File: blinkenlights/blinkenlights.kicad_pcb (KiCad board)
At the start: 4 copper layers, 160 x 100 mm, 114 parts, among them J201 Conn_03x32_Row_Letter_First, J202 Conn_02x20_Odd_Even, J203 Conn_02x20_Odd_Even, J204 Conn_02x20_Odd_Even, J205 Conn_02x20_Odd_Even, J301 Conn_01x01_Female, J302 Conn_01x01_Female, J303 Conn_01x01_Female, U201 AT24CS32-SSHM, U301 BD9C301FJ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

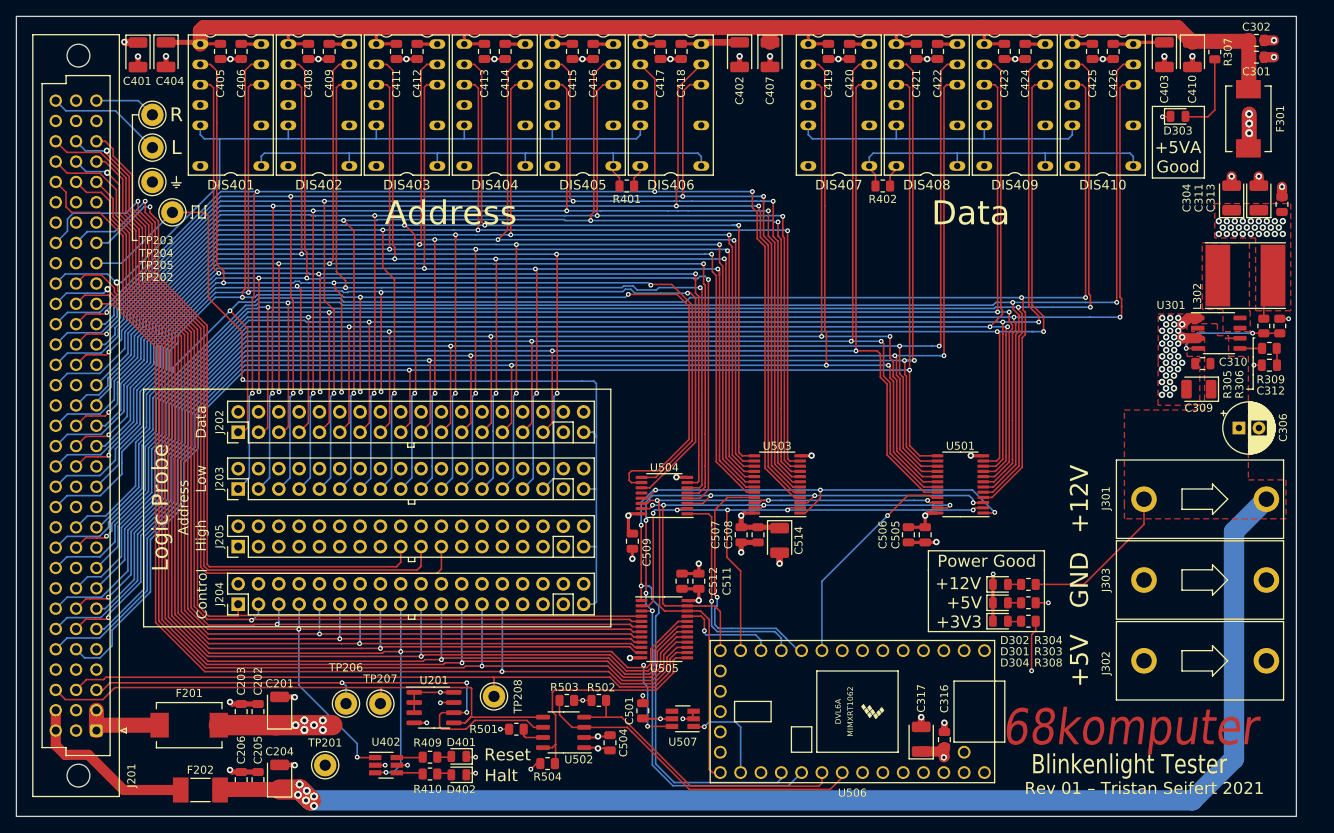
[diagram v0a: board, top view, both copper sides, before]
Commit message: Replaced many B case caps with A case
- There were sufficiently many 5V tantalum capcaitors on the
  blinkenlights board with the B case footprint (for 25V) rather than
  the A case (for 16V) assigned.
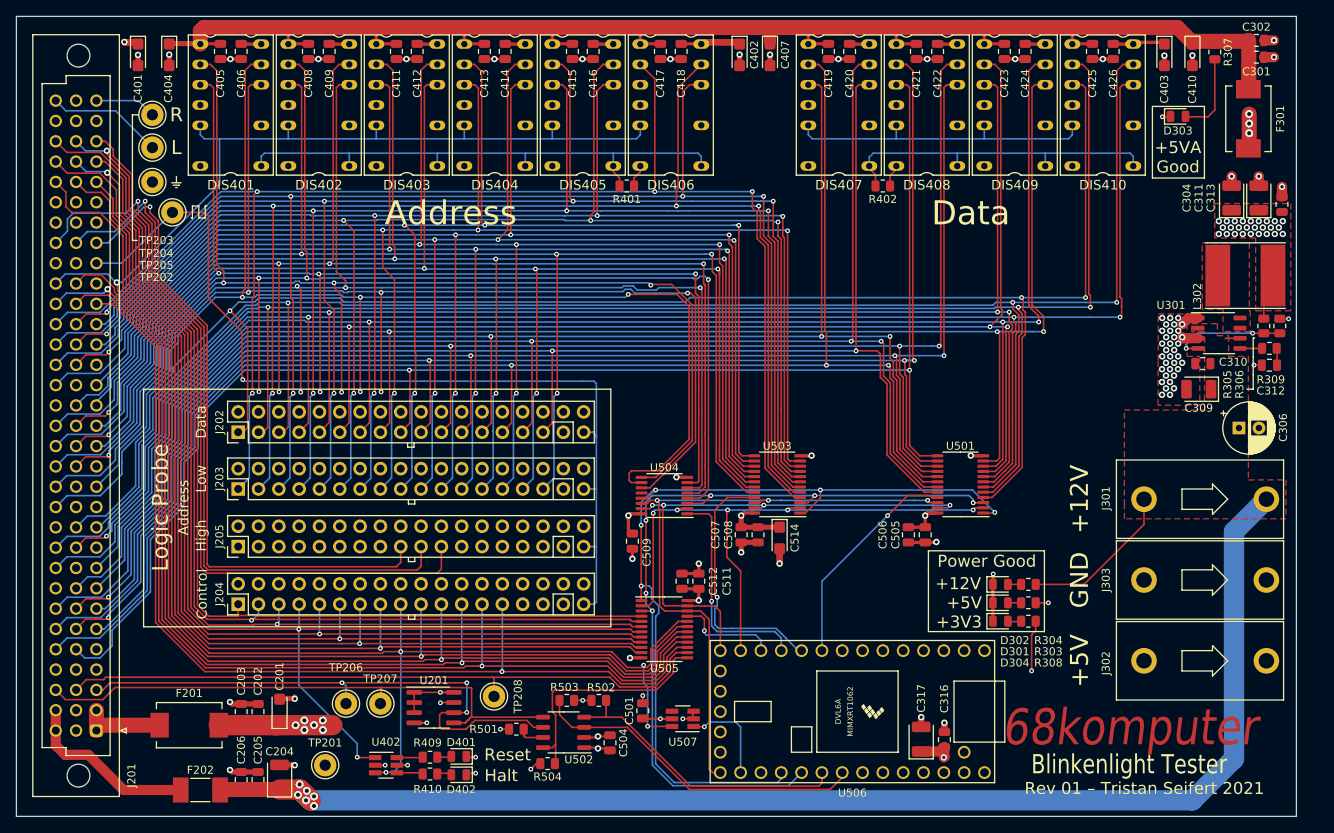
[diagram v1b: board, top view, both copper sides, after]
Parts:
- C201, C401, C402, C403, C404, C407, C410, C514: footprint Capacitor_Tantalum_SMD:CP_EIA-3528-21_Kemet-B -> Capacitor_Tantalum_SMD:CP_EIA-3216-18_Kemet-A
- moved C404 0.40 mm to (39.1, 24.8)
- moved C514 0.30 mm to (115.4, 85.2)
- moved C201 0.10 mm to (52.9, 106.7)

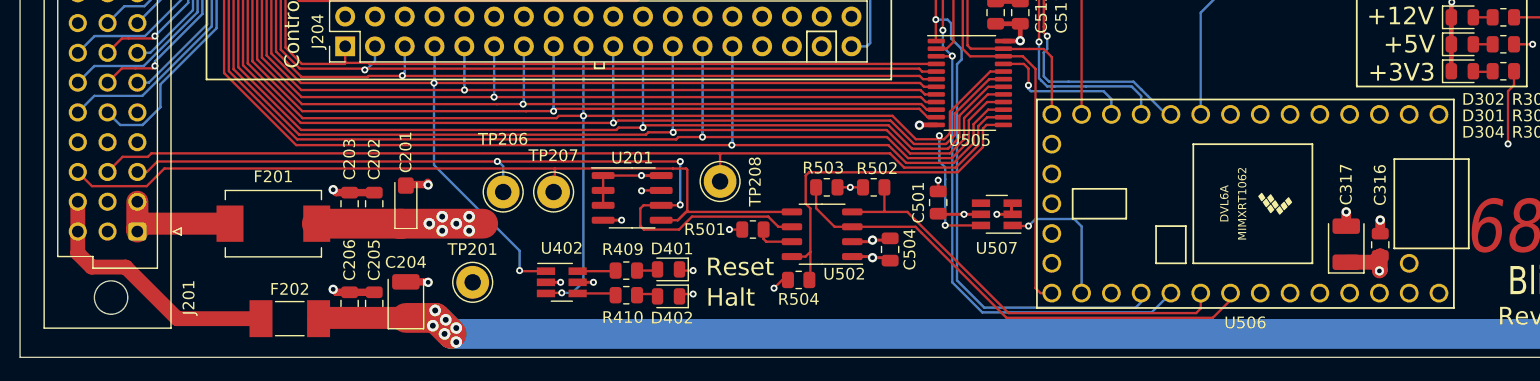
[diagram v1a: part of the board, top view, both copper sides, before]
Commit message: Some more direct IOs for blinkenlights
- /DTACK, /BERR, AS and R/W can be directly read/driven by Teensy GPIO;
  this should allow us to do bus transactions much faster since we can
  prepare the SPI transactions to set up the bus values, then control
  the bus timings most accurately.

- Fixed up a few incorrect pin directions for symbols used in the
  blinkenlights board
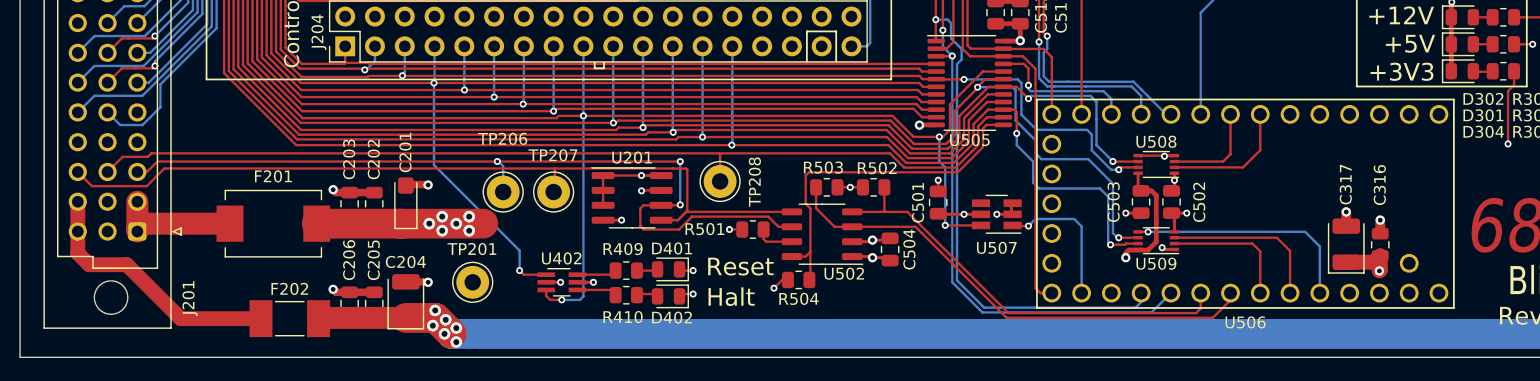
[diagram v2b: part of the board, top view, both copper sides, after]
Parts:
- added C502: 100nF, Capacitor_SMD:C_0805_2012Metric, F.Cu at (118.2, 106.8)
- added C503: 100nF, Capacitor_SMD:C_0805_2012Metric, F.Cu at (115.6, 106.8)
- added U508: 74LVC2T45DC, Package_SO:VSSOP-8_2.3x2mm_P0.5mm, F.Cu at (116.9, 103.5)
- added U509: 74LVC2T45DC, Package_SO:VSSOP-8_2.3x2mm_P0.5mm, F.Cu at (116.9, 110.0)
- U402: footprint Package_TO_SOT_SMD:SOT-23-6_Handsoldering -> Package_TO_SOT_SMD:SOT-363_SC-70-6_Handsoldering
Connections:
- U506 pad 27: unconnected-(U506-Pad27) -> /IO Drivers/R/~{W}_3V3
- U506 pad 28: unconnected-(U506-Pad28) -> /IO Drivers/~{AS_3V3}
- U506 pad 29: unconnected-(U506-Pad29) -> /IO Drivers/CTRL_DIR
- U506 pad 7: unconnected-(U506-Pad7) -> /IO Drivers/~{BERR_3V3}
- U506 pad 8: unconnected-(U506-Pad8) -> /IO Drivers/~{DTACK_3V3}
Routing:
- net /~{AS}: track 219.1 -> 242.8 mm, vias 2 -> 4
- net /~{BERR}: track 128.0 -> 150.9 mm, vias 1 -> 3
- net /R/~{W}: track 125.0 -> 146.3 mm, vias 1 -> 3
- net /IO Drivers/CTRL_DIR: track 0.00 -> 20.0 mm, vias 0 -> 1
- net /~{DTACK}: track 128.5 -> 145.0 mm, vias 1 -> 3
- net +5V: track 73.2 -> 87.9 mm, vias 41 -> 42
- net /IO Drivers/~{AS_3V3}: track 0.00 -> 13.9 mm
- net /IO Drivers/R/~{W}_3V3: track 0.00 -> 11.1 mm
- net /IO Drivers/~{BERR_3V3}: track 0.00 -> 11.0 mm
- net /IO Drivers/~{DTACK_3V3}: track 0.00 -> 8.43 mm
- net GND: track 104.6 -> 112.0 mm, vias 82 -> 85
- net +3V3: track 46.0 -> 48.6 mm, vias 9 -> 11
- net /~{HALT}: track 167.9 -> 169.2 mm

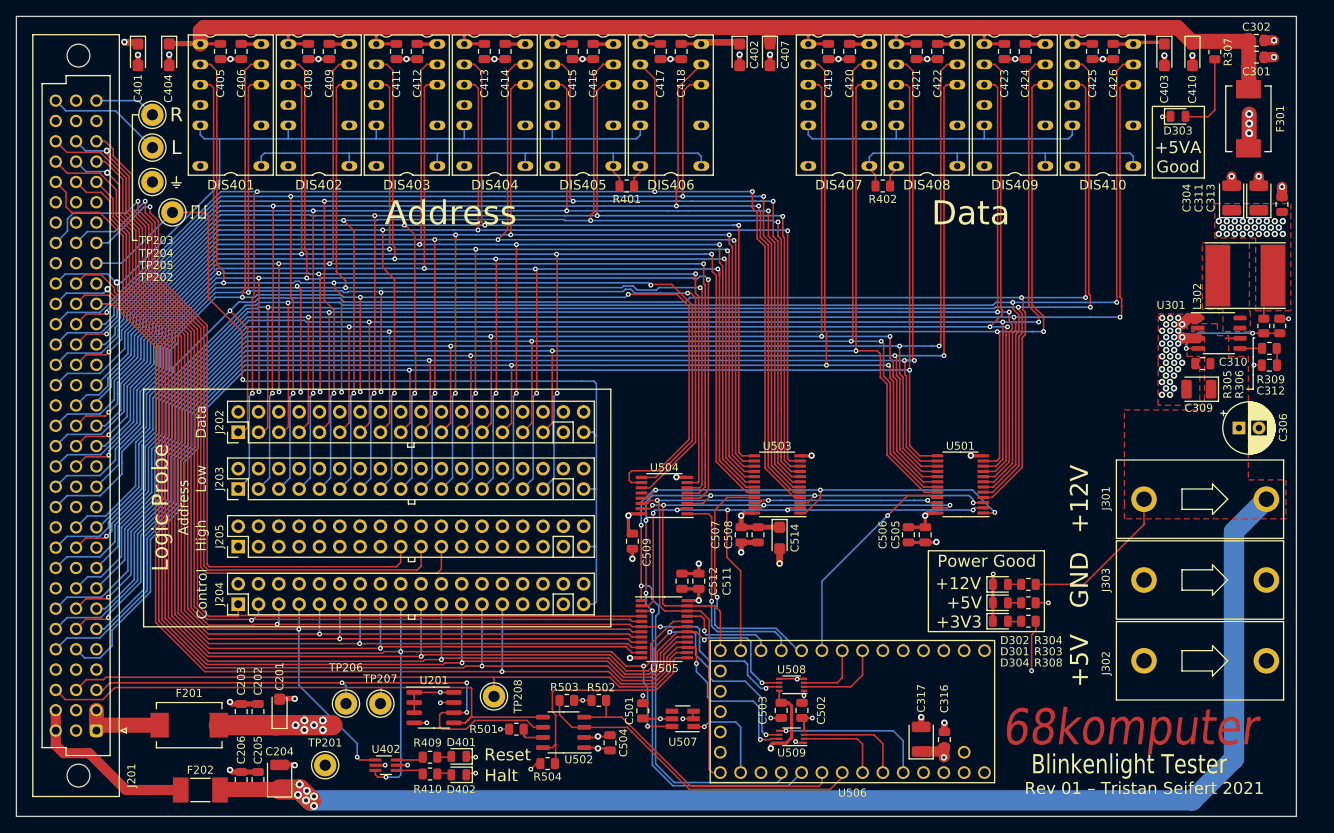
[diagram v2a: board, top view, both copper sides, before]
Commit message: Minor edits for manufacturability
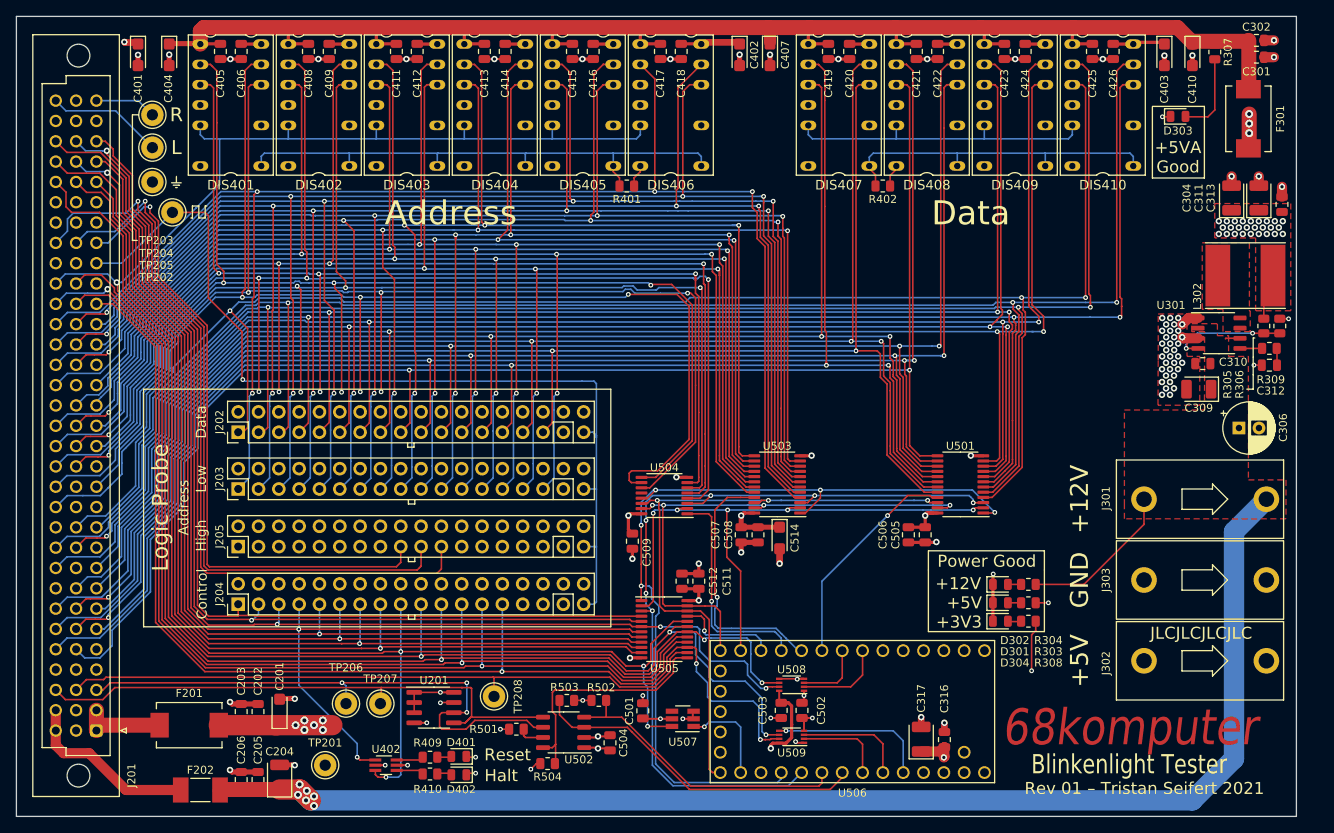
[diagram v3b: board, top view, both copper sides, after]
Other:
- board text added: "JLCJLCJLCJLC"
